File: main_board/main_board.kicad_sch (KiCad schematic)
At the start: 27 parts, among them J1 Conn_01x20, J2 Conn_01x20, J3 Conn_01x08_MountingPin, J4 Screw_Terminal_01x02, J5 Conn_01x06

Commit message: update main board schematics USB C and 3,3v regulator
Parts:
- removed J3: Conn_01x08_MountingPin, symbol Connector_Generic_MountingPin:Conn_01x08_MountingPin
- added J10: +VB, Connector_PinHeader_2.54mm:PinHeader_1x01_P2.54mm_Vertical, symbol Connector_Generic:Conn_01x01
- added J11: -VB, Connector_PinHeader_2.54mm:PinHeader_1x01_P2.54mm_Vertical, symbol Connector_Generic:Conn_01x01
- added J12: USB_C, Connector_USB:USB_C_Receptacle_GCT_USB4125-xx-x_6P_TopMnt_Horizontal, symbol Connector:USB_C_Receptacle_PowerOnly_6P
- added J3: LCD, Connector_PinSocket_2.54mm:PinSocket_1x08_P2.54mm_Vertical, symbol Connector_Generic:Conn_01x08
- added J6: DD0503MB Module, Connector_PinSocket_2.54mm:PinSocket_1x03_P2.54mm_Vertical, symbol Connector_Generic:Conn_01x03
- added J8: VIN_C, Connector_PinHeader_2.54mm:PinHeader_1x01_P2.54mm_Vertical, symbol Connector_Generic:Conn_01x01
- added J9: -VIN_C, Connector_PinHeader_2.54mm:PinHeader_1x01_P2.54mm_Vertical, symbol Connector_Generic:Conn_01x01
- added SW1: ON/OFF, Button_Switch_THT:SW_Slide_SPDT_Angled_CK_OS102011MA1Q, symbol Switch:SW_Wuerth_450301014042
- D2: value LED -> LED 1; footprint (none) -> LED_SMD:LED_1206_3216Metric
- D3: value LED -> LED 2; footprint (none) -> LED_SMD:LED_1206_3216Metric
- J1: value Conn_01x20 -> ESP32_LEFT; footprint (none) -> Connector_PinSocket_2.54mm:PinSocket_1x20_P2.54mm_Vertical
- J2: value Conn_01x20 -> ESP32_RIGHT; footprint (none) -> Connector_PinSocket_2.54mm:PinSocket_1x20_P2.54mm_Vertical
- J4: value Screw_Terminal_01x02 -> Battery Lipo 3,7v; footprint (none) -> Connector_JST:JST_EH_B2B-EH-A_1x02_P2.50mm_Vertical
- J5: value Conn_01x06 -> SD_CARD; footprint (none) -> Connector_PinSocket_2.54mm:PinSocket_1x06_P2.54mm_Vertical
- ON/OFF: renamed from D1; footprint (none) -> LED_SMD:LED_1206_3216Metric
- R1, R2, R3: value R_Small -> 130Ω; footprint (none) -> Resistor_SMD:R_0805_2012Metric
- R10, R11, R4, R5, R6, R7, R8, R9: value R_Small -> 10kΩ; footprint (none) -> Resistor_SMD:R_0805_2012Metric
- SW_A1: renamed from SW_A; value SW_Push -> ~; footprint (none) -> Button_Switch_THT:SW_PUSH_6mm
- SW_B1: renamed from SW_B; value SW_Push -> ~; footprint (none) -> Button_Switch_THT:SW_PUSH_6mm
- SW_DOWN1: renamed from SW_DOWN; value SW_Push -> ~; footprint (none) -> Button_Switch_THT:SW_PUSH_6mm
- SW_LEFT1: renamed from SW_LEFT; value SW_Push -> ~; footprint (none) -> Button_Switch_THT:SW_PUSH_6mm
- SW_RIGHT1: renamed from SW_RIGHT; value SW_Push -> ~; footprint (none) -> Button_Switch_THT:SW_PUSH_6mm
- SW_SELECT1: renamed from SW_SELECT; footprint (none) -> Button_Switch_THT:SW_PUSH_6mm
- SW_START1: renamed from SW_START; footprint (none) -> Button_Switch_THT:SW_PUSH_6mm
- SW_UP1: renamed from SW_UP; value SW_Push -> ~; footprint (none) -> Button_Switch_THT:SW_PUSH_6mm
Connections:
- net +3.3V: now also J3.1 (Pin_1), SW1.2 (C); no longer J4.1 (Pin_1)
- net GND: now also J11.1 (Pin_1), J3.2 (Pin_2), J6.2 (Pin_2)
- net GPIO10: now also J3.5 (Pin_5)
- net GPIO11: now also J3.3 (Pin_3)
- net GPIO12: now also J3.4 (Pin_4)
- net GPIO7: now also J3.8 (Pin_8)
- net GPIO8: now also J3.6 (Pin_6)
- net GPIO9: now also J3.7 (Pin_7)
- new net +VIN_charge: J12.A9 (VBUS), J12.B9 (VBUS), J8.1 (Pin_1)
- new net +Vb: J10.1 (Pin_1), J4.1 (Pin_1), J6.3 (Pin_3)
- new net -VIN_charge: J12.A12 (GND), J12.B12 (GND), J9.1 (Pin_1)
- new net Vout_reg: J6.1 (Pin_1), SW1.1 (B)
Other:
- moved on the sheet: J4

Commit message: update PCB -- finish routing pcb
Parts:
- renumbered ON/OFF to ON/OFF1
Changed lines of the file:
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@@
   (symbol (lib_id "Device:LED") (at 185.42 41.91 90) (unit 1)
     (in_bom yes) (on_board yes) (dnp no) (fields_autoplaced)
-    (property "Reference" "ON/OFF" (at 189.23 42.2275 90)
+    (property "Reference" "ON/OFF1" (at 189.23 42.2275 90)
       (effects (font (size 1.27 1.27)) (justify right))
     )
@@
       (project "main_board"
         (path "/1dcb963c-2272-4e5a-a1ca-affe3e5a9836"
-          (reference "ON/OFF") (unit 1)
+          (reference "ON/OFF1") (unit 1)
         )
       )

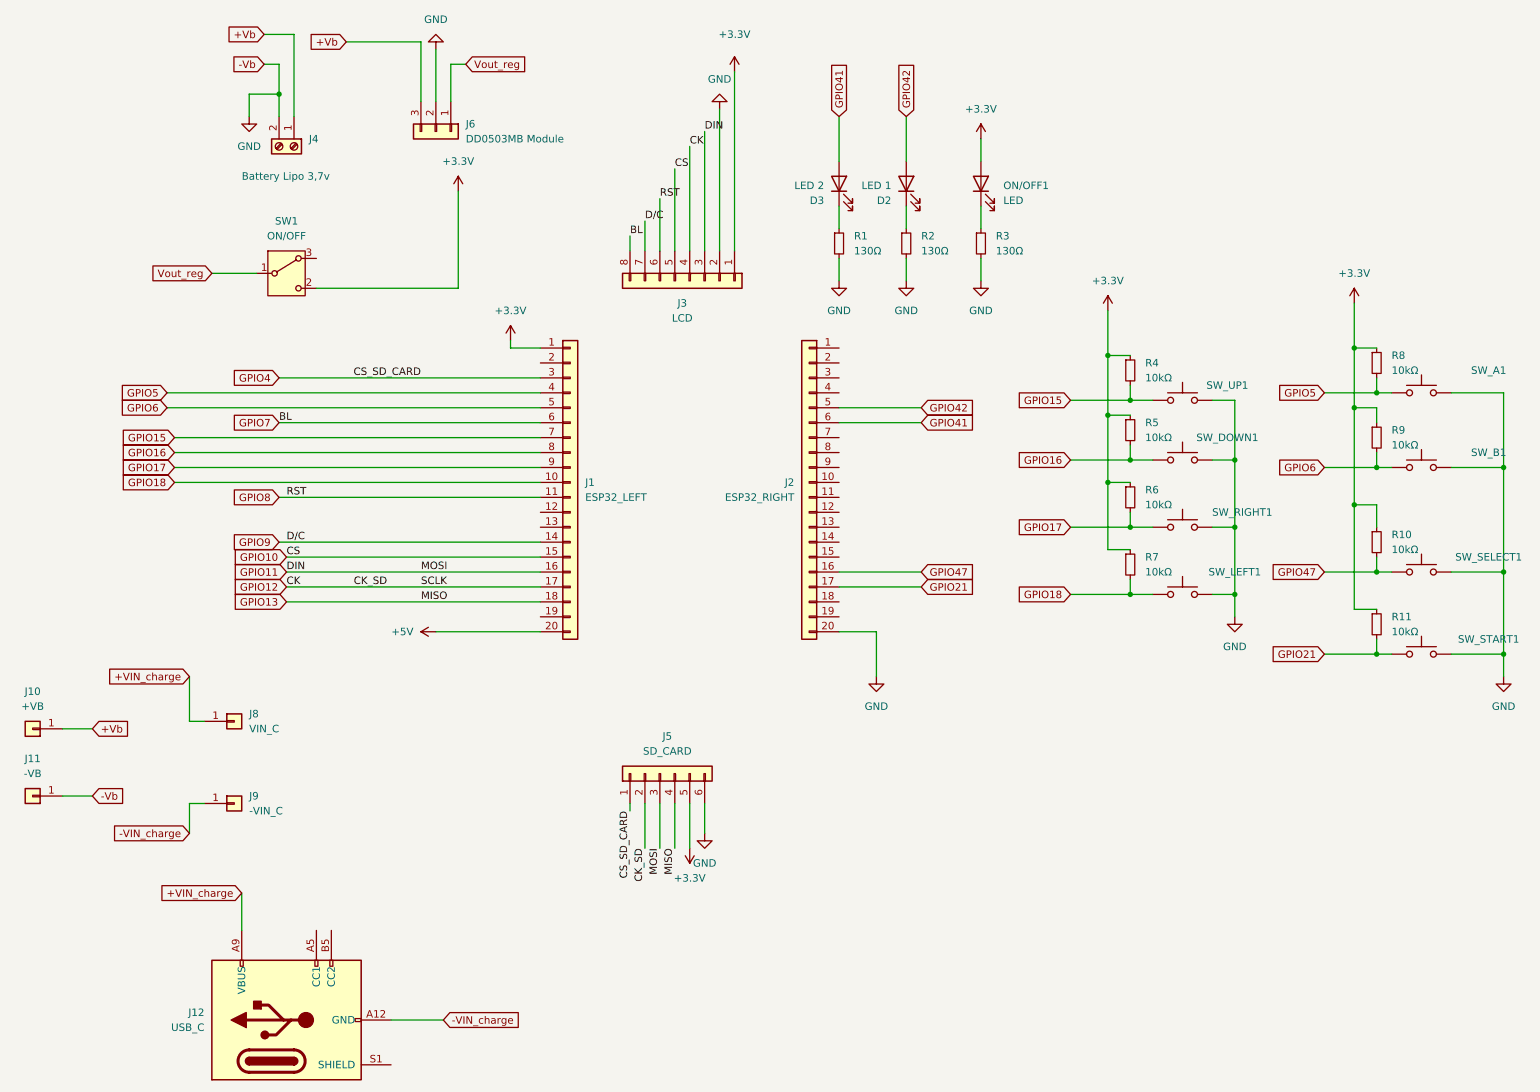
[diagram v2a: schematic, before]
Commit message: change LCD , correct charger board footprint and PSP mode
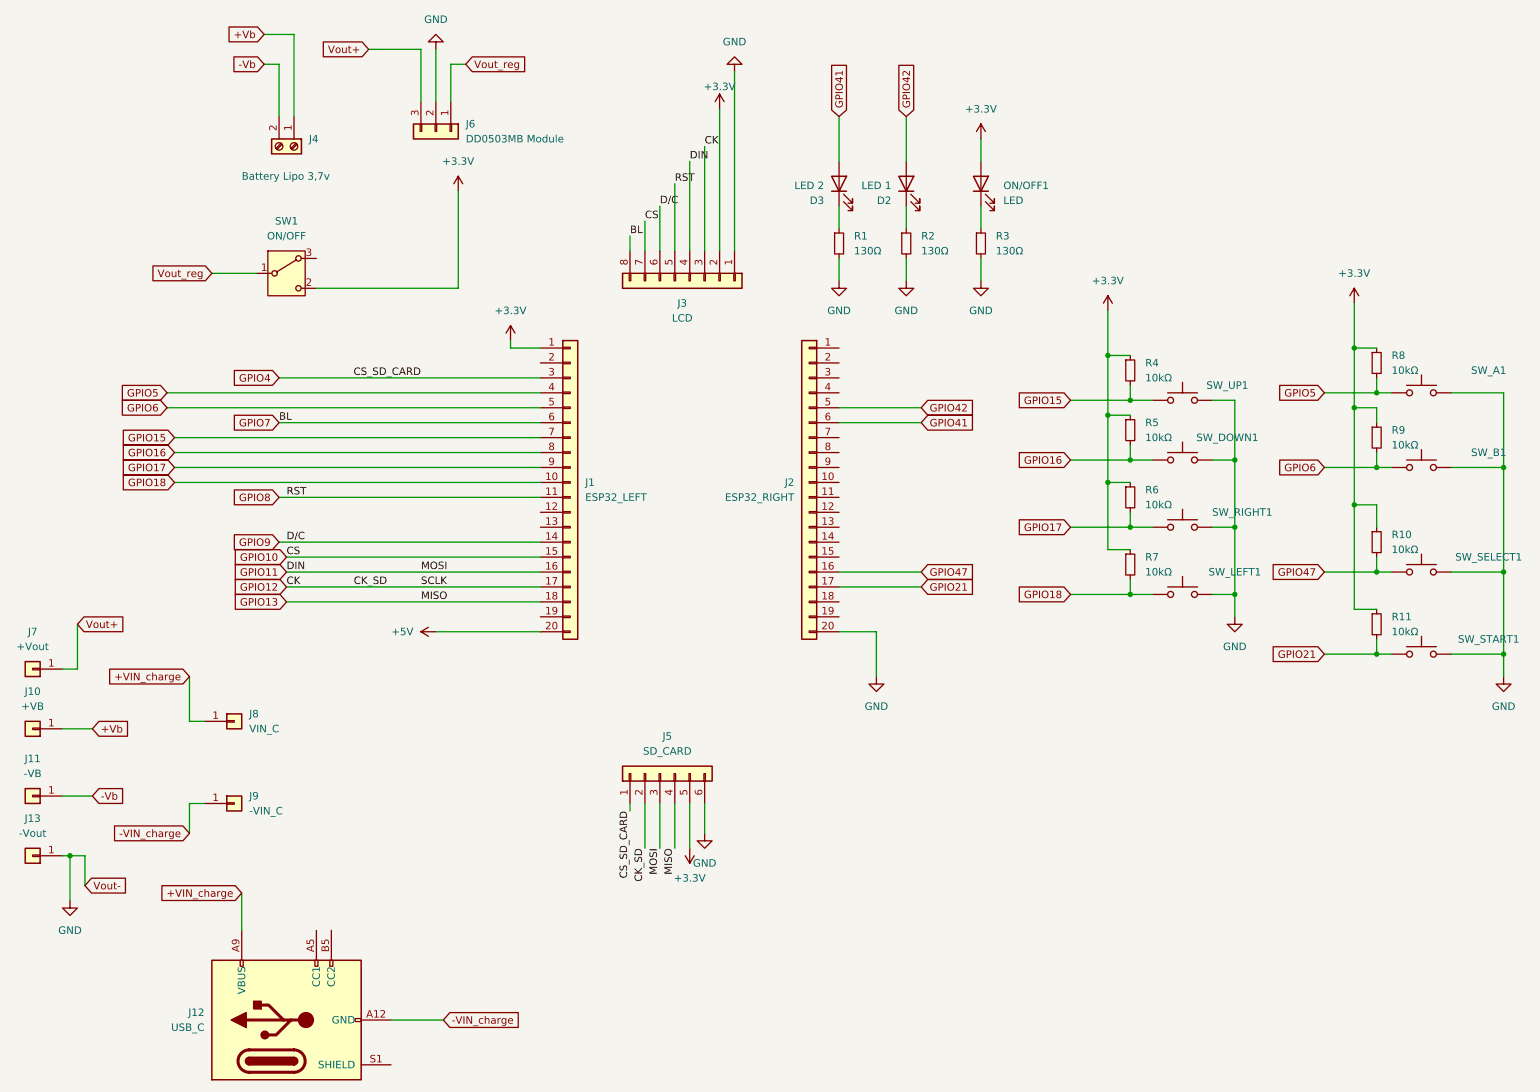
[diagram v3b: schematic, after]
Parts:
- added J13: -Vout, Connector_PinHeader_2.54mm:PinHeader_1x01_P2.54mm_Vertical, symbol Connector_Generic:Conn_01x01
- added J7: +Vout, Connector_PinHeader_2.54mm:PinHeader_1x01_P2.54mm_Vertical, symbol Connector_Generic:Conn_01x01
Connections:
- net +3.3V: now also J3.2 (Pin_2); no longer J3.1 (Pin_1)
- net +Vb: no longer J6.3 (Pin_3)
- net GND: now also J3.1 (Pin_1), J13.1 (Pin_1); no longer J11.1 (Pin_1), J3.2 (Pin_2), J4.2 (Pin_2)
- net GPIO10: now also J3.7 (Pin_7); no longer J3.5 (Pin_5)
- net GPIO11: now also J3.4 (Pin_4); no longer J3.3 (Pin_3)
- net GPIO12: now also J3.3 (Pin_3); no longer J3.4 (Pin_4)
- net GPIO8: now also J3.5 (Pin_5); no longer J3.6 (Pin_6)
- net GPIO9: now also J3.6 (Pin_6); no longer J3.7 (Pin_7)
- new net -Vb: J11.1 (Pin_1), J4.2 (Pin_2)
- new net Vout+: J6.3 (Pin_3), J7.1 (Pin_1)
